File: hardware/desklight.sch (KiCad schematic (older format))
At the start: 10 parts, among them IC1 ATTINY10-TS, P1 AVR_TPI, P2 Pwr5V1500mA, P3 WS2812_CON, SW1 Rotary_Encoder_Switch

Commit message: schematic cleanup
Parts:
- removed C1: C, symbol C
- removed C2, C3, C4: 100n, symbol C
- C5: footprint (none) -> Capacitors_SMD:C_0603_HandSoldering
- IC1: footprint SOT-23-6 -> TO_SOT_Packages_SMD:SOT-23-6_Handsoldering
- P1: footprint (none) -> Pin_Headers:Pin_Header_Straight_2x03_Pitch2.54mm
- P2: footprint (none) -> Pin_Headers:Pin_Header_Straight_1x02_Pitch2.54mm
- P3: footprint (none) -> Pin_Headers:Pin_Header_Straight_1x03_Pitch2.54mm
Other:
- moved on the sheet: P2, P3
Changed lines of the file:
@@
 F 0 "IC1" H 7300 4350 50  0000 C CNN
 F 1 "ATTINY10-TS" H 9150 3550 50  0000 C CNN
-F 2 "SOT-23-6" H 8300 4200 50  0000 C CIN
+F 2 "TO_SOT_Packages_SMD:SOT-23-6_Handsoldering" H 8300 4200 50  0001 C CIN
 F 3 "" H 8300 3950 50  0000 C CNN
 	1    8300 3950
@@
 F 0 "C5" H 9725 4050 50  0000 L CNN
 F 1 "100n" H 9725 3850 50  0000 L CNN
-F 2 "" H 9738 3800 50  0000 C CNN
+F 2 "Capacitors_SMD:C_0603_HandSoldering" H 9738 3800 50  0001 C CNN
 F 3 "" H 9700 3950 50  0000 C CNN
 	1    9700 3950
@@
 L CONN_01X02 P2
 U 1 1 588C12C5
-P 2200 2250
-F 0 "P2" H 2200 2400 50  0000 C CNN
-F 1 "Pwr5V1500mA" V 2300 2250 50  0000 C CNN
-F 2 "" H 2200 2250 50  0000 C CNN
-F 3 "" H 2200 2250 50  0000 C CNN
-	1    2200 2250
+P 2100 2250
+F 0 "P2" H 2100 2400 50  0000 C CNN
+F 1 "Pwr5V1500mA" V 2200 2250 50  0000 C CNN
+F 2 "Pin_Headers:Pin_Header_Straight_1x02_Pitch2.54mm" H 2100 2250 50  0001 C CNN
+F 3 "" H 2100 2250 50  0000 C CNN
+	1    2100 2250
 	1    0    0    1
 $EndComp
@@
 L PWR_FLAG #FLG03
 U 1 1 588C1337
-P 1650 1900
-F 0 "#FLG03" H 1650 1995 50  0001 C CNN
-F 1 "PWR_FLAG" H 1650 2080 50  0000 C CNN
-F 2 "" H 1650 1900 50  0000 C CNN
-F 3 "" H 1650 1900 50  0000 C CNN
-	1    1650 1900
+P 1600 2100
+F 0 "#FLG03" H 1600 2195 50  0001 C CNN
+F 1 "PWR_FLAG" H 1600 2280 50  0000 C CNN
+F 2 "" H 1600 2100 50  0000 C CNN
+F 3 "" H 1600 2100 50  0000 C CNN
+	1    1600 2100
 	1    0    0    -1
 $EndComp
@@
 L PWR_FLAG #FLG04
 U 1 1 588C135A
-P 1650 2600
-F 0 "#FLG04" H 1650 2695 50  0001 C CNN
-F 1 "PWR_FLAG" H 1650 2780 50  0000 C CNN
-F 2 "" H 1650 2600 50  0000 C CNN
-F 3 "" H 1650 2600 50  0000 C CNN
-	1    1650 2600
+P 1600 2400
+F 0 "#FLG04" H 1600 2495 50  0001 C CNN
+F 1 "PWR_FLAG" H 1600 2580 50  0000 C CNN
+F 2 "" H 1600 2400 50  0000 C CNN
+F 3 "" H 1600 2400 50  0000 C CNN
+	1    1600 2400
 	-1   0    0    1
 $EndComp
@@
 L GND #PWR05
 U 1 1 588C1377
-P 1300 2600
-F 0 "#PWR05" H 1300 2350 50  0001 C CNN
-F 1 "GND" H 1300 2450 50  0000 C CNN
-F 2 "" H 1300 2600 50  0000 C CNN
-F 3 "" H 1300 2600 50  0000 C CNN
-	1    1300 2600
+P 1250 2400
+F 0 "#PWR05" H 1250 2150 50  0001 C CNN
+F 1 "GND" H 1250 2250 50  0000 C CNN
+F 2 "" H 1250 2400 50  0000 C CNN
+F 3 "" H 1250 2400 50  0000 C CNN
+	1    1250 2400
 	1    0    0    -1
 $EndComp
@@
 L VCC #PWR06
 U 1 1 588C1394
-P 1300 1900
-F 0 "#PWR06" H 1300 1750 50  0001 C CNN
-F 1 "VCC" H 1300 2050 50  0000 C CNN
-F 2 "" H 1300 1900 50  0000 C CNN
-F 3 "" H 1300 1900 50  0000 C CNN
-	1    1300 1900
+P 1250 2100
+F 0 "#PWR06" H 1250 1950 50  0001 C CNN
+F 1 "VCC" H 1250 2250 50  0000 C CNN
+F 2 "" H 1250 2100 50  0000 C CNN
+F 3 "" H 1250 2100 50  0000 C CNN
+	1    1250 2100
 	1    0    0    -1
 $EndComp
@@
 F 0 "P1" H 1950 6200 50  0000 C CNN
 F 1 "AVR_TPI" H 1950 5800 50  0000 C CNN
-F 2 "" H 1950 4800 50  0000 C CNN
+F 2 "Pin_Headers:Pin_Header_Straight_2x03_Pitch2.54mm" H 1950 4800 50  0001 C CNN
 F 3 "" H 1950 4800 50  0000 C CNN
 	1    1950 6000
@@
 L CONN_01X03 P3
 U 1 1 588C1757
-P 6200 2900
-F 0 "P3" H 6200 3100 50  0000 C CNN
-F 1 "WS2812_CON" V 6300 2900 50  0000 C CNN
-F 2 "" H 6200 2900 50  0000 C CNN
-F 3 "" H 6200 2900 50  0000 C CNN
-	1    6200 2900
+P 6400 2900
+F 0 "P3" H 6400 3100 50  0000 C CNN
+F 1 "WS2812_CON" V 6500 2900 50  0000 C CNN
+F 2 "Pin_Headers:Pin_Header_Straight_1x03_Pitch2.54mm" H 6400 2900 50  0001 C CNN
+F 3 "" H 6400 2900 50  0000 C CNN
+	1    6400 2900
 	0    -1   -1   0
 $EndComp
@@
 L GND #PWR09
 U 1 1 588C17B4
-P 6100 3200
-F 0 "#PWR09" H 6100 2950 50  0001 C CNN
-F 1 "GND" H 6100 3050 50  0000 C CNN
-F 2 "" H 6100 3200 50  0000 C CNN
-F 3 "" H 6100 3200 50  0000 C CNN
-	1    6100 3200
+P 6300 3200
+F 0 "#PWR09" H 6300 2950 50  0001 C CNN
+F 1 "GND" H 6300 3050 50  0000 C CNN
+F 2 "" H 6300 3200 50  0000 C CNN
+F 3 "" H 6300 3200 50  0000 C CNN
+	1    6300 3200
 	1    0    0    -1
 $EndComp
@@
 L VCC #PWR010
 U 1 1 588C1829
-P 6400 3200
-F 0 "#PWR010" H 6400 3050 50  0001 C CNN
-F 1 "VCC" H 6400 3350 50  0000 C CNN
-F 2 "" H 6400 3200 50  0000 C CNN
-F 3 "" H 6400 3200 50  0000 C CNN
-	1    6400 3200
+P 6600 3200
+F 0 "#PWR010" H 6600 3050 50  0001 C CNN
+F 1 "VCC" H 6600 3350 50  0000 C CNN
+F 2 "" H 6600 3200 50  0000 C CNN
+F 3 "" H 6600 3200 50  0000 C CNN
+	1    6600 3200
 	0    1    1    0
 $EndComp
@@
 	1    0    0    -1
 $EndComp
-$Comp
-L C C4
-U 1 1 588C1BF7
-P 6700 4750
-F 0 "C4" H 6725 4850 50  0000 L CNN
-F 1 "100n" H 6725 4650 50  0000 L CNN
-F 2 "" H 6738 4600 50  0000 C CNN
-F 3 "" H 6700 4750 50  0000 C CNN
-	1    6700 4750
-	1    0    0    -1
-$EndComp
-$Comp
-L GND #PWR012
-U 1 1 588C2C7A
-P 6700 5000
-F 0 "#PWR012" H 6700 4750 50  0001 C CNN
-F 1 "GND" H 6700 4850 50  0000 C CNN
-F 2 "" H 6700 5000 50  0000 C CNN
-F 3 "" H 6700 5000 50  0000 C CNN
-	1    6700 5000
-	1    0    0    -1
-$EndComp
-Text Label 6200 3450 3    60   ~ 0
+Text Label 6400 3450 3    60   ~ 0
 DOUT
-$Comp
-L C C1
-U 1 1 588D4639
-P 1300 2250
-F 0 "C1" H 1325 2350 50  0000 L CNN
-F 1 "C" H 1325 2150 50  0000 L CNN
-F 2 "" H 1338 2100 50  0000 C CNN
-F 3 "" H 1300 2250 50  0000 C CNN
-	1    1300 2250
-	1    0    0    -1
-$EndComp
 $Comp
 L Rotary_Encoder_Switch SW1
@@
 	6700 4100 7100 4100
 Wire Wire Line
-	6100 3100 6100 3200
-Wire Wire Line
 	6300 3100 6300 3200
 Wire Wire Line
-	6300 3200 6400 3200
-Wire Wire Line
-	6200 3100 6200 3800
-Wire Wire Line
-	6200 3800 7100 3800
+	6500 3100 6500 3200
+Wire Wire Line
+	6500 3200 6600 3200
+Wire Wire Line
+	6400 3100 6400 3800
+Wire Wire Line
+	6400 3800 7100 3800
 Wire Notes Line
 	3350 500  3350 7750
@@
 	3350 4000 500  4000
 Wire Wire Line
-	1300 1900 1300 2100
-Wire Wire Line
-	1300 2400 1300 2600
-Wire Wire Line
-	1300 2500 1650 2500
-Wire Wire Line
-	1650 2300 1650 2600
-Connection ~ 1300 2500
-Wire Wire Line
-	1300 2000 1650 2000
-Wire Wire Line
-	1650 1900 1650 2200
-Connection ~ 1300 2000
-Wire Wire Line
-	1650 2200 2000 2200
-Connection ~ 1650 2000
-Wire Wire Line
-	1650 2300 2000 2300
-Connection ~ 1650 2500
+	1250 2100 1250 2200
+Wire Wire Line
+	1250 2300 1250 2400
+Wire Wire Line
+	1600 2300 1600 2400
+Wire Wire Line
+	1600 2100 1600 2200
+Wire Wire Line
+	1250 2200 1900 2200
+Wire Wire Line
+	1250 2300 1900 2300
 Wire Wire Line
 	6250 4500 6450 4500
@@
 	6250 4300 6700 4300
 Wire Wire Line
-	6700 4100 6700 4600
-Wire Wire Line
-	6700 5000 6700 4900
-Wire Wire Line
-	4800 3900 7100 3900
-Connection ~ 6700 4300
+	4900 3900 7100 3900
 Wire Wire Line
 	7100 4000 5100 4000
 Wire Wire Line
-	5100 4000 5100 4600
-Wire Wire Line
 	5100 4300 5650 4300
 Wire Wire Line
-	4800 3900 4800 4600
-Wire Wire Line
-	4800 4500 5650 4500
+	4900 4500 5650 4500
 Wire Wire Line
 	5650 4400 5400 4400
 $Comp
-L C C2
-U 1 1 58C9DD44
-P 4800 4750
-F 0 "C2" H 4825 4850 50  0000 L CNN
-F 1 "100n" H 4825 4650 50  0000 L CNN
-F 2 "" H 4838 4600 50  0000 C CNN
-F 3 "" H 4800 4750 50  0000 C CNN
-	1    4800 4750
-	1    0    0    -1
-$EndComp
-$Comp
-L C C3
-U 1 1 58C9DDBA
-P 5100 4750
-F 0 "C3" H 5125 4850 50  0000 L CNN
-F 1 "100n" H 5125 4650 50  0000 L CNN
-F 2 "" H 5138 4600 50  0000 C CNN
-F 3 "" H 5100 4750 50  0000 C CNN
-	1    5100 4750
-	1    0    0    -1
-$EndComp
-Connection ~ 5100 4300
-Connection ~ 4800 4500
-Wire Wire Line
-	4800 4900 4800 5000
-$Comp
-L GND #PWR013
-U 1 1 58C9E040
-P 5100 5000
-F 0 "#PWR013" H 5100 4750 50  0001 C CNN
-F 1 "GND" H 5100 4850 50  0000 C CNN
-F 2 "" H 5100 5000 50  0000 C CNN
-F 3 "" H 5100 5000 50  0000 C CNN
-	1    5100 5000
-	1    0    0    -1
-$EndComp
-Wire Wire Line
-	5100 5000 5100 4900
-$Comp
-L GND #PWR015
-U 1 1 58C9ED0D
-P 4800 5000
-F 0 "#PWR015" H 4800 4750 50  0001 C CNN
-F 1 "GND" H 4800 4850 50  0000 C CNN
-F 2 "" H 4800 5000 50  0000 C CNN
-F 3 "" H 4800 5000 50  0000 C CNN
-	1    4800 5000
-	1    0    0    -1
-$EndComp
-$Comp
-L GND #PWR014
+L GND #PWR012
 U 1 1 58C9ECDB
 P 5400 5000
-F 0 "#PWR014" H 5400 4750 50  0001 C CNN
+F 0 "#PWR012" H 5400 4750 50  0001 C CNN
 F 1 "GND" H 5400 4850 50  0000 C CNN
 F 2 "" H 5400 5000 50  0000 C CNN
@@
 Wire Wire Line
 	5400 4400 5400 5000
+Wire Wire Line
+	6700 4300 6700 4100
+Wire Wire Line
+	5100 4000 5100 4300
+Wire Wire Line
+	4900 4500 4900 3900
+Connection ~ 1600 2200
+Connection ~ 1600 2300
 $EndSCHEMATC

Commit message: basic pcb design
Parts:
- SW1: footprint (none) -> projectspecifics:Encoder_PEC11R
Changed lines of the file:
@@
 F 0 "SW1" H 5950 4660 50  0000 C CNN
 F 1 "Rotary_Encoder_Switch" H 5950 4140 50  0000 C CNN
-F 2 "" H 5850 4560 50  0001 C CNN
+F 2 "projectspecifics:Encoder_PEC11R" H 5850 4560 50  0001 C CNN
 F 3 "" H 5950 4660 50  0001 C CNN
 	1    5950 4400

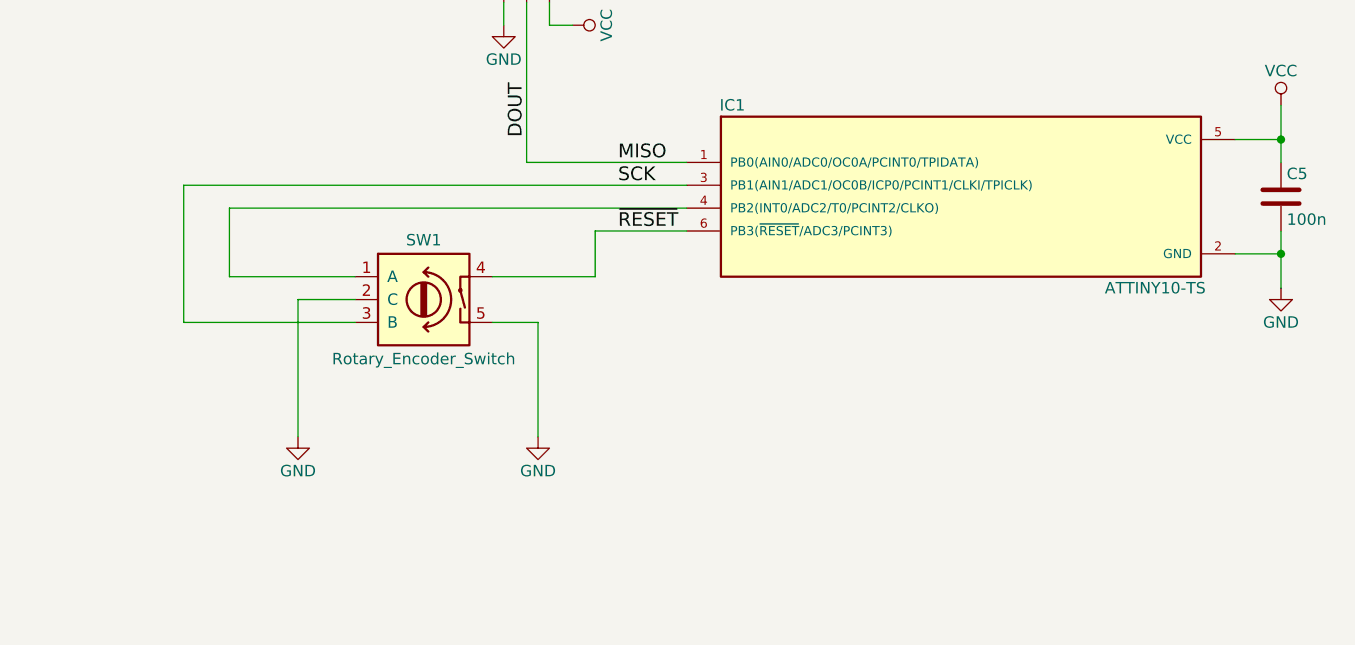
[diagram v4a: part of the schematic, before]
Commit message: add debouncing caps
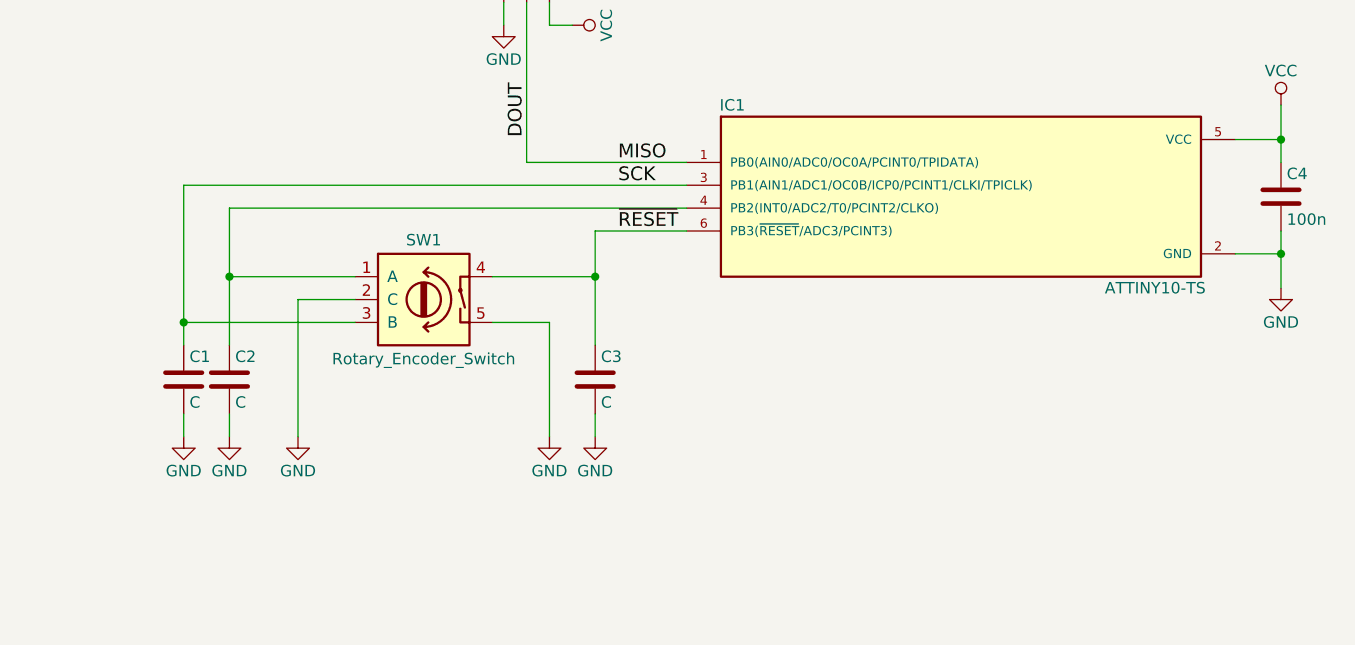
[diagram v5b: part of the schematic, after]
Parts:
- added C1, C2, C3: C, Capacitors_SMD:C_0603_HandSoldering, symbol C
- renumbered C5 to C4
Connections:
- net GND: now also C1.2, C2.2, C3.2
- net SCK: now also C1.1
- net ~RESET: now also C3.1
- net at IC1.4 (PB2(INT0/ADC2/T0/PCINT2/CLKO)), SW1.1 (A): now also C2.1
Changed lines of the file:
@@
 $EndComp
 $Comp
-L C C5
+L C C4
 U 1 1 588C115D
 P 9700 3950
-F 0 "C5" H 9725 4050 50  0000 L CNN
+F 0 "C4" H 9725 4050 50  0000 L CNN
 F 1 "100n" H 9725 3850 50  0000 L CNN
 F 2 "Capacitors_SMD:C_0603_HandSoldering" H 9738 3800 50  0001 C CNN
@@
 L GND #PWR011
 U 1 1 588C1BAB
-P 6450 5000
-F 0 "#PWR011" H 6450 4750 50  0001 C CNN
-F 1 "GND" H 6450 4850 50  0000 C CNN
-F 2 "" H 6450 5000 50  0000 C CNN
-F 3 "" H 6450 5000 50  0000 C CNN
-	1    6450 5000
+P 6500 5000
+F 0 "#PWR011" H 6500 4750 50  0001 C CNN
+F 1 "GND" H 6500 4850 50  0000 C CNN
+F 2 "" H 6500 5000 50  0000 C CNN
+F 3 "" H 6500 5000 50  0000 C CNN
+	1    6500 5000
 	1    0    0    -1
 $EndComp
@@
 	1    0    0    -1
 $EndComp
-Wire Wire Line
-	9500 3700 9700 3700
-Wire Wire Line
-	9700 3550 9700 3800
-Wire Wire Line
-	9700 4100 9700 4350
-Wire Wire Line
-	9700 4200 9500 4200
-Connection ~ 9700 3700
-Connection ~ 9700 4200
-Wire Wire Line
-	2200 5900 2300 5900
-Wire Wire Line
-	2300 5900 2300 5800
-Wire Wire Line
-	2200 6100 2300 6100
-Wire Wire Line
-	2300 6100 2300 6200
-Wire Wire Line
-	1700 5900 1400 5900
-Wire Wire Line
-	1700 6000 1400 6000
-Wire Wire Line
-	1700 6100 1400 6100
-Wire Wire Line
-	6700 4100 7100 4100
-Wire Wire Line
-	6300 3100 6300 3200
-Wire Wire Line
-	6500 3100 6500 3200
-Wire Wire Line
-	6500 3200 6600 3200
-Wire Wire Line
-	6400 3100 6400 3800
-Wire Wire Line
-	6400 3800 7100 3800
-Wire Notes Line
-	3350 500  3350 7750
-Wire Notes Line
-	3350 4000 500  4000
-Wire Wire Line
-	1250 2100 1250 2200
-Wire Wire Line
-	1250 2300 1250 2400
-Wire Wire Line
-	1600 2300 1600 2400
-Wire Wire Line
-	1600 2100 1600 2200
-Wire Wire Line
-	1250 2200 1900 2200
-Wire Wire Line
-	1250 2300 1900 2300
-Wire Wire Line
-	6250 4500 6450 4500
-Wire Wire Line
-	6450 4500 6450 5000
-Wire Wire Line
-	6250 4300 6700 4300
-Wire Wire Line
-	4900 3900 7100 3900
-Wire Wire Line
-	7100 4000 5100 4000
-Wire Wire Line
-	5100 4300 5650 4300
-Wire Wire Line
-	4900 4500 5650 4500
-Wire Wire Line
-	5650 4400 5400 4400
 $Comp
 L GND #PWR012
@@
 	1    0    0    -1
 $EndComp
+$Comp
+L C C3
+U 1 1 596939D7
+P 6700 4750
+F 0 "C3" H 6725 4850 50  0000 L CNN
+F 1 "C" H 6725 4650 50  0000 L CNN
+F 2 "Capacitors_SMD:C_0603_HandSoldering" H 6738 4600 50  0001 C CNN
+F 3 "" H 6700 4750 50  0001 C CNN
+	1    6700 4750
+	1    0    0    -1
+$EndComp
+Wire Wire Line
+	9500 3700 9700 3700
+Wire Wire Line
+	9700 3550 9700 3800
+Wire Wire Line
+	9700 4100 9700 4350
+Wire Wire Line
+	9700 4200 9500 4200
+Connection ~ 9700 3700
+Connection ~ 9700 4200
+Wire Wire Line
+	2200 5900 2300 5900
+Wire Wire Line
+	2300 5900 2300 5800
+Wire Wire Line
+	2200 6100 2300 6100
+Wire Wire Line
+	2300 6100 2300 6200
+Wire Wire Line
+	1700 5900 1400 5900
+Wire Wire Line
+	1700 6000 1400 6000
+Wire Wire Line
+	1700 6100 1400 6100
+Wire Wire Line
+	6700 4100 7100 4100
+Wire Wire Line
+	6300 3100 6300 3200
+Wire Wire Line
+	6500 3100 6500 3200
+Wire Wire Line
+	6500 3200 6600 3200
+Wire Wire Line
+	6400 3100 6400 3800
+Wire Wire Line
+	6400 3800 7100 3800
+Wire Notes Line
+	3350 500  3350 7750
+Wire Notes Line
+	3350 4000 500  4000
+Wire Wire Line
+	1250 2100 1250 2200
+Wire Wire Line
+	1250 2300 1250 2400
+Wire Wire Line
+	1600 2300 1600 2400
+Wire Wire Line
+	1600 2100 1600 2200
+Wire Wire Line
+	1250 2200 1900 2200
+Wire Wire Line
+	1250 2300 1900 2300
+Wire Wire Line
+	6250 4500 6500 4500
+Wire Wire Line
+	6250 4300 6700 4300
+Wire Wire Line
+	4900 3900 7100 3900
+Wire Wire Line
+	7100 4000 5100 4000
+Wire Wire Line
+	5100 4300 5650 4300
+Wire Wire Line
+	4900 4500 5650 4500
+Wire Wire Line
+	5650 4400 5400 4400
 Wire Wire Line
 	5400 4400 5400 5000
 Wire Wire Line
-	6700 4300 6700 4100
-Wire Wire Line
-	5100 4000 5100 4300
-Wire Wire Line
-	4900 4500 4900 3900
+	6700 4100 6700 4600
+Wire Wire Line
+	5100 4000 5100 4600
+Wire Wire Line
+	4900 3900 4900 4600
 Connection ~ 1600 2200
 Connection ~ 1600 2300
+Connection ~ 6700 4300
+Wire Wire Line
+	6500 4500 6500 5000
+$Comp
+L C C1
+U 1 1 59693BDB
+P 4900 4750
+F 0 "C1" H 4925 4850 50  0000 L CNN
+F 1 "C" H 4925 4650 50  0000 L CNN
+F 2 "Capacitors_SMD:C_0603_HandSoldering" H 4938 4600 50  0001 C CNN
+F 3 "" H 4900 4750 50  0001 C CNN
+	1    4900 4750
+	1    0    0    -1
+$EndComp
+$Comp
+L C C2
+U 1 1 59693C1C
+P 5100 4750
+F 0 "C2" H 5125 4850 50  0000 L CNN
+F 1 "C" H 5125 4650 50  0000 L CNN
+F 2 "Capacitors_SMD:C_0603_HandSoldering" H 5138 4600 50  0001 C CNN
+F 3 "" H 5100 4750 50  0001 C CNN
+	1    5100 4750
+	1    0    0    -1
+$EndComp
+Connection ~ 5100 4300
+Connection ~ 4900 4500
+Wire Wire Line
+	4900 4900 4900 5000
+Wire Wire Line
+	5100 4900 5100 5000
+$Comp
+L GND #PWR013
+U 1 1 59693D3B
+P 5100 5000
+F 0 "#PWR013" H 5100 4750 50  0001 C CNN
+F 1 "GND" H 5100 4850 50  0000 C CNN
+F 2 "" H 5100 5000 50  0001 C CNN
+F 3 "" H 5100 5000 50  0001 C CNN
+	1    5100 5000
+	1    0    0    -1
+$EndComp
+$Comp
+L GND #PWR014
+U 1 1 59693D61
+P 4900 5000
+F 0 "#PWR014" H 4900 4750 50  0001 C CNN
+F 1 "GND" H 4900 4850 50  0000 C CNN
+F 2 "" H 4900 5000 50  0001 C CNN
+F 3 "" H 4900 5000 50  0001 C CNN
+	1    4900 5000
+	1    0    0    -1
+$EndComp
+Wire Wire Line
+	6700 4900 6700 5000
+$Comp
+L GND #PWR015
+U 1 1 59693EE7
+P 6700 5000
+F 0 "#PWR015" H 6700 4750 50  0001 C CNN
+F 1 "GND" H 6700 4850 50  0000 C CNN
+F 2 "" H 6700 5000 50  0001 C CNN
+F 3 "" H 6700 5000 50  0001 C CNN
+	1    6700 5000
+	1    0    0    -1
+$EndComp
 $EndSCHEMATC
